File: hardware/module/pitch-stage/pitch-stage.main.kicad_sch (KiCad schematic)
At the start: 13 parts

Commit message: WIP module schematics: footprints, bought-part fields, and the two board projects (module-main, module-jack)
Recovered from a container restart; not yet exported or checked.

Co-Authored-By: Claude Opus 5.5 <noreply@anthropic.com>
Claude-Session: https://claude.ai/code/session_01LmB4muFXnoLprWX4JzuJ5A
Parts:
- C-AA-PITCH, C-FILT-PITCH: footprint (none) -> Capacitor_SMD:C_0805_2012Metric; Assembly (none) -> machine; LCSC (none) -> C27071; MPN (none) -> CL21C103JBFNNNE; Manufacturer (none) -> Samsung Electro-Mechanics
- C-DEC-PITCH-NEG, C-DEC-PITCH-POS: footprint (none) -> Capacitor_SMD:C_0805_2012Metric; Assembly (none) -> machine; LCSC (none) -> C49678; MPN (none) -> CC0805KRX7R9BB104; Manufacturer (none) -> YAGEO
- C-FB-PITCH: footprint (none) -> Capacitor_SMD:C_0805_2012Metric; Assembly (none) -> machine; LCSC (none) -> C28260; MPN (none) -> CL21C222JBFNNNE; Manufacturer (none) -> Samsung Electro-Mechanics
- D-JACK-CLAMP: footprint (none) -> Package_TO_SOT_SMD:SOT-23; Assembly (none) -> machine; LCSC (none) -> C2500; MPN (none) -> BAV99,215; Manufacturer (none) -> Nexperia
- R-BIAS-DAC: footprint (none) -> Resistor_SMD:R_0805_2012Metric; Assembly (none) -> machine; LCSC (none) -> C149504; MPN (none) -> 0805W8F1003T5E; Manufacturer (none) -> UNI-ROYAL(Uniroyal Elec)
- R-OPAMP-IN: footprint (none) -> Resistor_SMD:R_0805_2012Metric; Assembly (none) -> machine; LCSC (none) -> C17513; MPN (none) -> 0805W8F1001T5E; Manufacturer (none) -> UNI-ROYAL(Uniroyal Elec)
- R-OUT-PROT: footprint (none) -> Resistor_SMD:R_1206_3216Metric; Assembly (none) -> machine; LCSC (none) -> C4261071; MPN (none) -> ERJ-P08F1001V; Manufacturer (none) -> Panasonic
- RN-PITCH: footprint (none) -> Package_SO:MSOP-8-1EP_3x3mm_P0.65mm_EP1.68x1.88mm; Assembly (none) -> hand; Manufacturer (none) -> Analog Devices
- TRIM-GAIN: footprint (none) -> Potentiometer_THT:Potentiometer_Bourns_3296W_Vertical; Assembly (none) -> hand; LCSC (none) -> C83685; MPN (none) -> 3296W-1-201LF; Manufacturer (none) -> Bourns
- TRIM-OFFSET: footprint (none) -> Potentiometer_THT:Potentiometer_Bourns_3296W_Vertical; Assembly (none) -> hand; LCSC (none) -> C34846; MPN (none) -> 3296W-1-103LF; Manufacturer (none) -> Bourns
- U-PITCH: footprint (none) -> Package_SO:SOIC-8_3.9x4.9mm_P1.27mm; Assembly (none) -> machine; LCSC (none) -> C139363; MPN (none) -> OPA2197IDR; Manufacturer (none) -> Texas Instruments

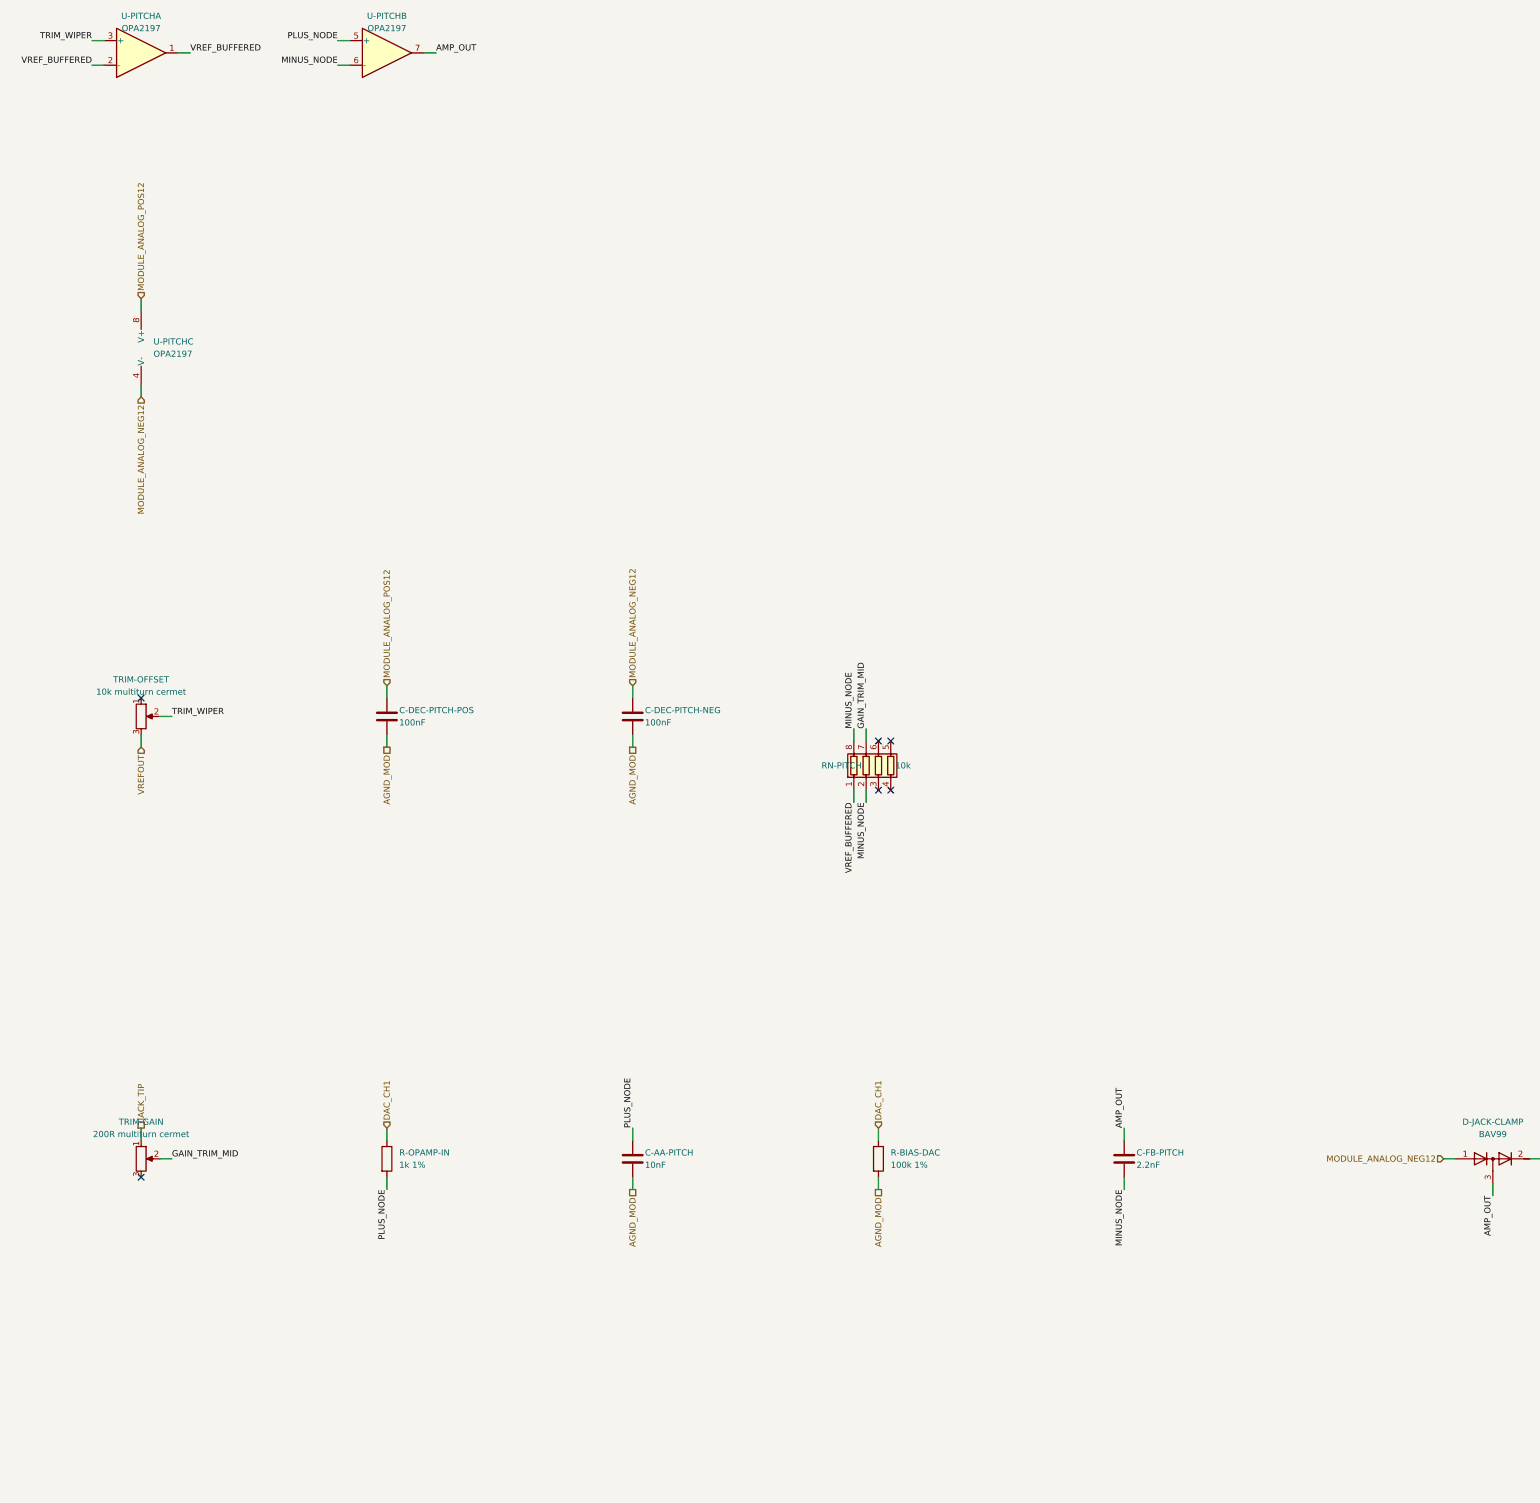
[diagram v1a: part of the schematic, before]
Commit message: Module: D3 turned round; pitch trims made buildable and bipolar; LT5400 pad and order code; breath-zero range resistor
D3 (the -12 V entry diode) was netlisted anode-to-bus, reverse-biased in
normal running (found by the analog sims): cathode to the bus now.
TRIM-OFFSET spans VREFOUT-AGND and injects through R-VREF-INJ against
R-VREF-SER into the follower at gain 1.02 (R-VREF-FB/R-VREF-GND): 2.500 V at
mid-travel, -60/+50 mV. It also holds the 3-state VREFOUT at 0 V while the
DAC's reference is disabled. TRIM-GAIN is centred by R-GAIN-CTR in the R1 leg
(+/-1 %) and its CW end strapped to the wiper. RN-PITCH carries its exposed
pad as pin 9 to AGND_MOD, spares tied down; ordered LT5400BIMS8E-1#PBF.
R-OPAMP-IN is six; R-TRIM-RANGE split into real parts. R-ZERO-TOP gives
TRIM-BREATH-ZERO the 0-1.0 V range its page specifies. Page text follows.

Co-Authored-By: Claude Opus 5.5 <noreply@anthropic.com>
Claude-Session: https://claude.ai/code/session_01LmB4muFXnoLprWX4JzuJ5A
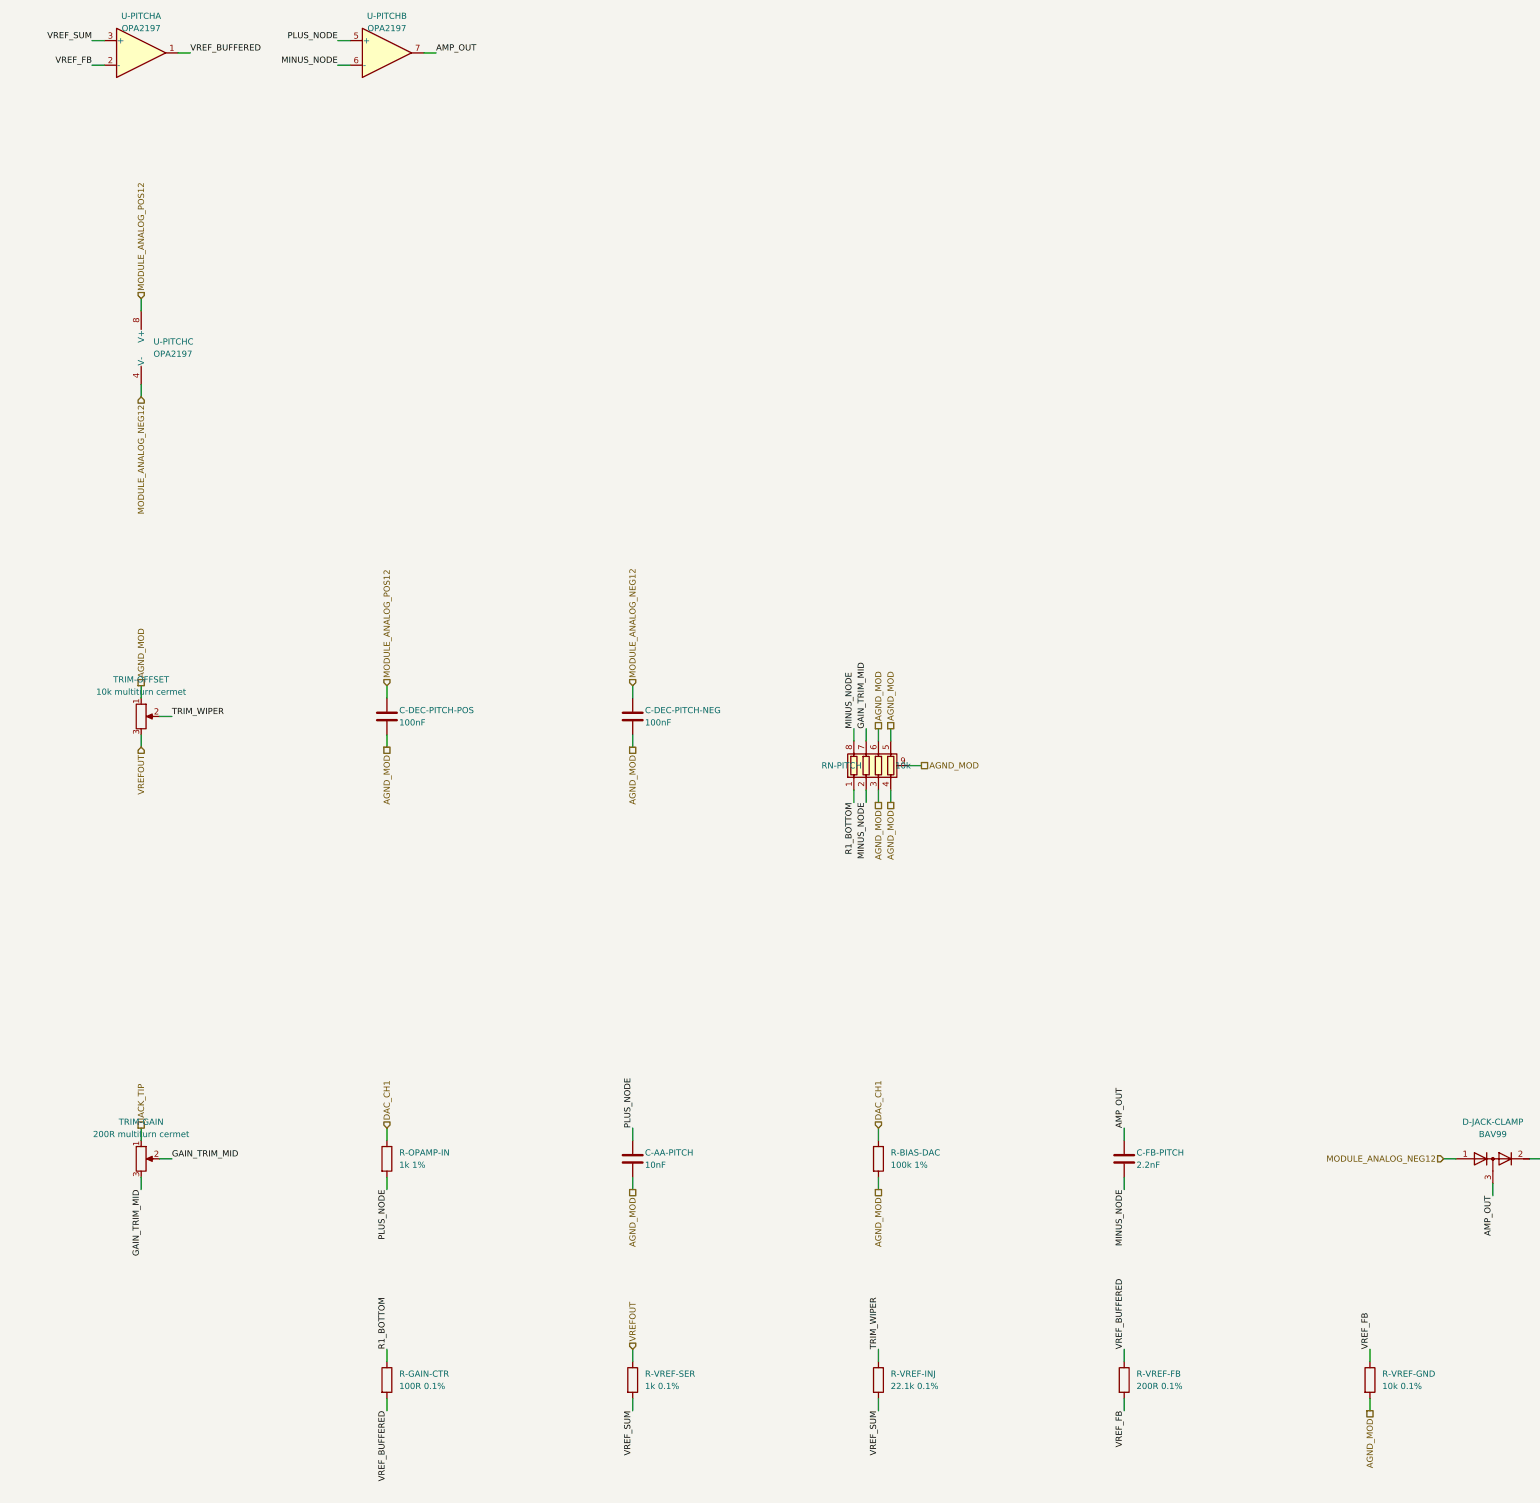
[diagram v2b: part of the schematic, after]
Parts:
- added R-GAIN-CTR: 100R 0.1%, Resistor_SMD:R_0805_2012Metric, symbol Device:R
- added R-VREF-FB: 200R 0.1%, Resistor_SMD:R_0805_2012Metric, symbol Device:R
- added R-VREF-GND: 10k 0.1%, Resistor_SMD:R_0805_2012Metric, symbol Device:R
- added R-VREF-INJ: 22.1k 0.1%, Resistor_SMD:R_0805_2012Metric, symbol Device:R
- added R-VREF-SER: 1k 0.1%, Resistor_SMD:R_0805_2012Metric, symbol Device:R
- RN-PITCH: LCSC (none) -> C42416907; MPN (none) -> LT5400BIMS8E-1#PBF; Note R1 (R1A-R1B) and R2 (R2A-R2B) are the page's R1 = R2 that make gain exactly 2 and the intercept exactly -2.500 V from one ratio. R3 and R4 are spare. The exposed pad is not a pin here: where it goes is open (R-PRECISION row) -> R1 (R1A-R1B) and R2 (R2A-R2B) are the page's R1 = R2 that make gain exactly 2 and the intercept exactly -2.500 V from one ratio. R3 and R4 are spare, both ends on AGND_MOD. THE EXPOSED PAD (EP, pin 9) GOES TO AGND_MOD, the quiet analog ground the datasheet asks for (LT5400.pdf p.6); it is the dominant stray on the 1 V/oct network, 5.5 pF to the resistors; Pins R1A=1(R1.1) R1B=8(R1.2) R2A=2(R2.1) R2B=7(R2.2) R3A=3(R3.1) R3B=6(R3.2) R4A=4(R4.1) R4B=5(R4.2) -> R1A=1(R1.1) R1B=8(R1.2) R2A=2(R2.1) R2B=7(R2.2) R3A=3(R3.1) R3B=6(R3.2) R4A=4(R4.1) R4B=5(R4.2) EP=9(EP); Pins_source datasheets/analog/LT5400.pdf p.2 pin configuration (MS8E): R1 1-8, R2 2-7, R3 3-6, R4 4-5; the exposed pad (pin 9, floating) is not on this symbol - where it goes is open (R-PRECISION row) -> datasheets/analog/LT5400.pdf p.2 pin configuration (MS8E): R1 1-8, R2 2-7, R3 3-6, R4 4-5, exposed pad pin 9 (floating); the embedded symbol carries pin 9 as EP to match the MSOP-8-1EP footprint's pad 9
- TRIM-GAIN: Note IN SERIES with R2, between R2 and the jack. One-sided 0 to 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 -> IN SERIES with R2, between R2 and the jack, its CW end stra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
- TRIM-OFFSET: Note AHEAD of the follower, so it scales V_ref and therefore the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 -> Across VREFOUT (CW) and AGND_MOD (CCW); its wiper injects i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
- U-PITCH: Note Half A is the unity follower on the trimmed reference - the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 -> Half A buffers the trimmed reference at gain 1.02 (R-VREF-F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
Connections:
- net AGND_MOD: now also RN-PITCH.3 (R3.1), RN-PITCH.4 (R4.1), RN-PITCH.5 (R4.2), RN-PITCH.6 (R3.2), RN-PITCH.9 (EP), TRIM-OFFSET.1, R-VREF-GND.2
- net GAIN_TRIM_MID: now also TRIM-GAIN.3
- net TRIM_WIPER: now also R-VREF-INJ.1; no longer U-PITCH.3 (+)
- net VREFOUT: now also R-VREF-SER.1
- net VREF_BUFFERED: now also R-GAIN-CTR.2, R-VREF-FB.1; no longer RN-PITCH.1 (R1.1), U-PITCH.2 (-)
- new net R1_BOTTOM: R-GAIN-CTR.1, RN-PITCH.1 (R1.1)
- new net VREF_FB: R-VREF-FB.2, R-VREF-GND.1, U-PITCH.2 (-)
- new net VREF_SUM: R-VREF-INJ.2, R-VREF-SER.2, U-PITCH.3 (+)
- no-connect marks 6 -> 0

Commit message: #32: checkpoint - the owner's three answers and side-adjust trimmers
Owner decisions of 2026-10-04, recorded in ADR 0003/0004/0023/0024:
- WIDE's CMRR requirement band is DC to 7 kHz ("Keep 10 kHz, accept");
  cmrr-wide holds 58.5 dB there and records 10 kHz.
- D-TVS-BREATH is the PESD12VL1BA (19 pF), datasheet banked; PWR_GND
  held under -60 dB in each mode's band, WIDE at the accepted figure.
- The -12 V offset leg is filtered: R-BREATH-OFFNEG-A/-B 47.5k with
  C-BREATH-OFFNEG 1 uF at the split (6.7 Hz). Rest level +16 mV.
- The four trimmers are Bourns 3296X side-adjust, set with the module
  out of the rack; no rear-access windows. Current 3296 datasheet banked.

Sims are mid-run; their results land in the next commit.

Gate-Red: sim results stale or pre-change for receive-stage, power-entry, pitch-stage, mod-channels, shaper, system, breath-excitation-reference, digital-and-supervision and panel-led while they re-run on these inputs (checkpoint, as asked every 45 min); module-main and main-board .kicad_pcb parity with the new/changed parts (layout's, not touched here); main-board fab stale against the breath-adc sheet; module-main's existing routing/silk/acid-trap failures.

Co-Authored-By: Claude Opus 5.5 <noreply@anthropic.com>
Claude-Session: https://claude.ai/code/session_01LmB4muFXnoLprWX4JzuJ5A
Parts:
- TRIM-GAIN: footprint Potentiometer_THT:Potentiometer_Bourns_3296W_Vertical -> Potentiometer_THT:Potentiometer_Bourns_3296X_Horizontal; LCSC C83685 -> C111787; MPN 3296W-1-201LF -> 3296X-1-201LF
- TRIM-OFFSET: footprint Potentiometer_THT:Potentiometer_Bourns_3296W_Vertical -> Potentiometer_THT:Potentiometer_Bourns_3296X_Horizontal; LCSC C34846 -> C111776; MPN 3296W-1-103LF -> 3296X-1-103LF
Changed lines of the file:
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@@
     (property "Reference" "TRIM-OFFSET" (at 40.64 180.34 0) (effects (font (size 1.27 1.27))))
     (property "Value" "10k multiturn cermet" (at 40.64 182.88 0) (effects (font (size 1.27 1.27))))
-    (property "Footprint" "Potentiometer_THT:Potentiometer_Bourns_3296W_Vertical" (at 40.64 187.96 0) (effects (font (size 1.27 1.27)) hide))
+    (property "Footprint" "Potentiometer_THT:Potentiometer_Bourns_3296X_Horizontal" (at 40.64 187.96 0) (effects (font (size 1.27 1.27)) hide))
     (property "Datasheet" "" (at 40.64 187.96 0) (effects (font (size 1.27 1.27)) hide))
     (property "Row" "TRIM-OFFSET" (at 40.64 187.96 0) (effects (font (size 1.27 1.27)) hide))
@@
     (property "Pins_source" "datasheets/discrete-and-power/BOURNS-3296-TRIMPOT.pdf p.1 circuit: 1 CCW, 2 wiper, 3 CW" (at 40.64 187.96 0) (effects (font (size 1.27 1.27)) hide))
     (property "Manufacturer" "Bourns" (at 40.64 187.96 0) (effects (font (size 1.27 1.27)) hide))
-    (property "MPN" "3296W-1-103LF" (at 40.64 187.96 0) (effects (font (size 1.27 1.27)) hide))
-    (property "LCSC" "C34846" (at 40.64 187.96 0) (effects (font (size 1.27 1.27)) hide))
+    (property "MPN" "3296X-1-103LF" (at 40.64 187.96 0) (effects (font (size 1.27 1.27)) hide))
+    (property "LCSC" "C111776" (at 40.64 187.96 0) (effects (font (size 1.27 1.27)) hide))
     (property "Assembly" "hand" (at 40.64 187.96 0) (effects (font (size 1.27 1.27)) hide))
     (pin "1")
@@
     (property "Reference" "TRIM-GAIN" (at 40.64 271.78 0) (effects (font (size 1.27 1.27))))
     (property "Value" "200R multiturn cermet" (at 40.64 274.32 0) (effects (font (size 1.27 1.27))))
-    (property "Footprint" "Potentiometer_THT:Potentiometer_Bourns_3296W_Vertical" (at 40.64 279.4 0) (effects (font (size 1.27 1.27)) hide))
+    (property "Footprint" "Potentiometer_THT:Potentiometer_Bourns_3296X_Horizontal" (at 40.64 279.4 0) (effects (font (size 1.27 1.27)) hide))
     (property "Datasheet" "" (at 40.64 279.4 0) (effects (font (size 1.27 1.27)) hide))
     (property "Row" "TRIM-GAIN" (at 40.64 279.4 0) (effects (font (size 1.27 1.27)) hide))
@@
     (property "Pins_source" "datasheets/discrete-and-power/BOURNS-3296-TRIMPOT.pdf p.1 circuit: 1 CCW, 2 wiper, 3 CW" (at 40.64 279.4 0) (effects (font (size 1.27 1.27)) hide))
     (property "Manufacturer" "Bourns" (at 40.64 279.4 0) (effects (font (size 1.27 1.27)) hide))
-    (property "MPN" "3296W-1-201LF" (at 40.64 279.4 0) (effects (font (size 1.27 1.27)) hide))
-    (property "LCSC" "C83685" (at 40.64 279.4 0) (effects (font (size 1.27 1.27)) hide))
+    (property "MPN" "3296X-1-201LF" (at 40.64 279.4 0) (effects (font (size 1.27 1.27)) hide))
+    (property "LCSC" "C111787" (at 40.64 279.4 0) (effects (font (size 1.27 1.27)) hide))
     (property "Assembly" "hand" (at 40.64 279.4 0) (effects (font (size 1.27 1.27)) hide))
     (pin "1")
